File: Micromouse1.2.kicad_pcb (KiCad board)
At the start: 2 copper layers, 42 x 17 mm, 113 parts, among them J1 USB_B, P1 CONN_01X4, U1 BAT54C, U10 2X3Header, U11 ULN2003APWR, U12 SMT_0540-S-R, U13 splitter, U14 ferrite, U15 LMZ21701, U16 JST_Connector, U17 Switch_micromouse, U18 LMZ21701, U19 splitter, U2 TC4427, U20 TPD3S014, U21 MKL02Z32VFG4, U22 LP38691, U23 MK66FX1M0, U24 Test_Point, U25 Test_Point, U26 Test_Point, U27 Test_Point, U28 Test_Point, U29 Test_Point, U3 ferrite, U30 Test_Point, U4 TC4427, U5 ferrite, U6 BAT54C, U7 ZXMHC3F381N8, U8 ZXMHC3F381N8, U9 2X3Header, Y1 Crystal_16MHz, Y2 32.768MHz

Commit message: finished floor planning
-replaced the TC4427 and H brige by a single DRV8833 chip
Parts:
- removed C3: 0.1uF, Capacitors_SMD:C_0603
- removed D7: D, Diodes_SMD:D_0603
- removed U12: SMT_0540-S-R, micromouse:Buzzer_SMT-0540-S-R
- removed U4: TC4427, micromouse:TC4427_MSOP8
- removed U7, U8: ZXMHC3F381N8, micromouse:ZXMHC3F381N8
- added C32: 10nF, Capacitors_SMD:C_0603, F.Cu at (122.6, 71.3)
- added C33: 0.1uF, Capacitors_SMD:C_0603, F.Cu at (122.6, 69.8)
- added C34: C, Capacitors_SMD:C_0603, F.Cu at (118.6, 67.7)
- added C35: C, Capacitors_SMD:C_0402, F.Cu at (118.8, 124.5)
- added U31: MPU-6500, micromouse:MPU-6500, F.Cu at (118.7, 70.7)
- added U32: Motor_mount, micromouse:Motor_mount, F.Cu at (140.3, 87.3)
- C1: value 0.1uF -> 100uF
- C10, C12: footprint Resistors_SMD:R_0805 -> micromouse:R_0805
- C11, C14, C17, C21, C22, C23, C25, C26, C28: footprint Capacitors_SMD:C_0402 -> micromouse:C_0402
- C13, C15: footprint Capacitors_SMD:C_0805 -> micromouse:C_0805
- C16, C18, C19, C24, C27, C29, U3: footprint Capacitors_SMD:C_0402 -> micromouse:C_0603
- C2: value 100uF -> 10uF; footprint Capacitors_SMD:C_0603 -> Capacitors_SMD:C_0805
- C20: footprint Capacitors_SMD:C_1206 -> micromouse:C_1206
- C4: value 100uF -> 0.1uF
- D1, D2, D3, D4, D5, D6: footprint micromouse:IR-Reciver -> micromouse:IR_Reciver
- D10, D11, D12, D13, D8, D9: footprint micromouse:IR-Emitter -> micromouse:IR_Emitter
- J1: footprint micromouse:USB_B -> micromouse:USB_Micro-B
- R1, R2, R3, R4, R5, R6, R7, R8: footprint Resistors_SMD:R_0603 -> Capacitors_SMD:C_0402
- R15, R16, R17, R18, R19, R20: footprint Resistors_SMD:R_0603 -> micromouse:C_0402
- R21, R22, R23, R25, R26, R27, R39, R40: footprint Resistors_SMD:R_0402 -> micromouse:R_0402
- R24, R28, R29: footprint Resistors_SMD:R_0603 -> micromouse:R_0603
- U11: footprint micromouse:ULN2003APWR -> micromouse:ULN2003V12
- U13: value splitter -> Motor_mount; footprint micromouse:spliter -> micromouse:Motor_mount
- U14, U5: footprint Capacitors_SMD:C_0402 -> micromouse:R_0402
- U15: footprint MicromouseFootprint:LMZ21701 -> micromouse:LMZ21701
- U16: footprint Capacitors_SMD:C_0402 -> micromouse:JST_Connector
- U2: value TC4427 -> DRV8833; footprint micromouse:TC4427_MSOP8 -> micromouse:DRV8833
- moved R28 152.6 mm to (101.4, 76.7)
- moved R29 152.4 mm to (101.5, 71.8), turned to 180 degrees
- moved U13 146.4 mm to (97.3, 87.3), turned to 270 degrees
- moved R24 118.9 mm to (135.0, 76.2), turned to 90 degrees
- moved U19 77.9 mm to (134.1, 103.8), turned to 90 degrees
- moved C6 63.7 mm to (110.3, 45.3)
- moved P1 63.5 mm to (25.5, 58.6), turned to 270 degrees
- moved J1 52.4 mm to (133.0, 110.1), turned to 0 degrees
- moved C9 51.9 mm to (118.1, 38.0)
- moved D6 51.4 mm to (151.8, 59.9), turned to 174.7 degrees
- moved C8 51.1 mm to (119.5, 38.0), turned to 270 degrees
- moved D1 49.5 mm to (88.1, 59.2), turned to 184.3 degrees
- moved D8 46.9 mm to (93.5, 56.0), turned to 184.3 degrees
- moved C12 46.8 mm to (131.4, 71.4), turned to 180 degrees
- moved U24 46.3 mm to (134.2, 71.6), turned to 180 degrees
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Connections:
- C1 pad 1: V_BAT -> VBAT
- C1 pad 2: GNDM -> GNDD
- C2 pad 1: V_BAT -> VBAT
- C2 pad 2: GNDM -> GNDD
- C21 pad 2: GND -> GNDD
- C22 pad 2: GND -> GNDD
- C23 pad 2: GND -> GNDD
- C25 pad 2: GND -> GNDD
- C27 pad 2: GND -> GNDD
- C29 pad 2: GND -> GNDD
- C30 pad 1: V3.3 -> V1.8
- C31 pad 1: V3.3 -> V1.8
- C4 pad 1: V_BAT -> VBAT
- C4 pad 2: GNDM -> GNDD
- C6 pad 1: V3.3 -> V1.8
- C7 pad 1: V3.3 -> V1.8
- C8 pad 1: V3.3 -> V1.8
- C9 pad 1: V3.3 -> V1.8
- D10 pad 2: V3.3 -> V1.8
- D11 pad 2: V3.3 -> V1.8
- D12 pad 2: V3.3 -> V1.8
- D13 pad 2: V3.3 -> V1.8
- D8 pad 2: V3.3 -> V1.8
- D9 pad 2: V3.3 -> V1.8
- J1 pad 1: Net-(C16-Pad1) -> Net-(J1-Pad1)
- J1 pad 4: GND -> Net-(J1-Pad4)
- J1 pad 5: GND -> Net-(J1-Pad5)
- L1 pad 1: Net-(C15-Pad1) -> Net-(L1-Pad1)
- P1 pad 3: GND -> Net-(P1-Pad3)
- R29 pad 1: Net-(L1-Pad2) -> Net-(R29-Pad1)
- R37 pad 2: Net-(J1-Pad3) -> Net-(R37-Pad2)
- R38 pad 2: Net-(J1-Pad2) -> Net-(R38-Pad2)
- R5 pad 1: Net-(R1-Pad1) -> Net-(R3-Pad1)
- R6 pad 1: Net-(R3-Pad1) -> GNDD
- R6 pad 2: GNDD -> Net-(R2-Pad1)
- R7 pad 1: Net-(R2-Pad1) -> Net-(R4-Pad1)
- R8 pad 1: Net-(R4-Pad1) -> GNDD
- R8 pad 2: GNDD -> Net-(R1-Pad1)
- U1 pad 1: Net-(C17-Pad1) -> Net-(C22-Pad1)
- U1 pad 2: Net-(C22-Pad1) -> Net-(U1-Pad2)
- U1 pad 3: Net-(U1-Pad3) -> Net-(C17-Pad1)
- U19 pad 2: Net-(U19-Pad2) -> GNDA
- U2 pad 1: Net-(U2-Pad1) -> Net-(R30-Pad1)
- U2 pad 2: Net-(R1-Pad1) -> Net-(U2-Pad2)
- U2 pad 3: GNDM -> Net-(U10-Pad4)
- U2 pad 4: Net-(R2-Pad1) -> Net-(R30-Pad1)
- U2 pad 5: Net-(U2-Pad5) -> Net-(U10-Pad3)
- U2 pad 6: V_BAT -> Net-(U2-Pad6)
- U2 pad 7: Net-(U2-Pad7) -> Net-(R3-Pad1)
- U2 pad 8: Net-(U2-Pad8) -> Net-(R4-Pad1)
- U20 pad 1: Net-(C21-Pad1) -> Net-(R40-Pad1)
- U20 pad 3: Net-(R40-Pad1) -> Net-(C21-Pad1)
- U22 pad 2: GND -> GNDD
- U26 pad 1: Net-(L1-Pad2) -> Net-(R29-Pad1)
- U27 pad 1: Net-(R1-Pad1) -> Net-(R2-Pad1)
- U28 pad 1: Net-(R3-Pad1) -> Net-(R4-Pad1)
- U29 pad 1: Net-(R2-Pad1) -> Net-(R1-Pad1)
- U30 pad 1: Net-(R4-Pad1) -> Net-(R3-Pad1)
- U6 pad 1: Net-(C21-Pad1) -> Net-(U3-Pad2)
- U6 pad 3: Net-(U3-Pad2) -> Net-(C21-Pad1)
- U9 pad 3: Net-(U7-Pad2) -> Net-(U2-Pad16)
- U9 pad 4: Net-(U7-Pad6) -> Net-(U2-Pad2)
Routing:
- net Net-(C22-Pad1): track 0.00 -> 34.6 mm, vias 0 -> 1
- net GNDD: track 1.20 -> 35.2 mm, vias 4 -> 5
- net Net-(R37-Pad1): track 0.00 -> 16.0 mm
- net Net-(U20-Pad6): track 0.00 -> 15.8 mm, vias 0 -> 2
- net Net-(C28-Pad1): track 0.00 -> 13.8 mm, vias 0 -> 1
- net Net-(U23-PadM7): track 0.00 -> 11.5 mm
- net GNDM: track 10.9 -> 0.00 mm
- net Net-(U7-Pad6): track 10.8 -> 0.00 mm
- net Net-(C21-Pad1): track 0.00 -> 10.3 mm
- net Net-(U10-Pad4): track 10.2 -> 0.00 mm
- net Net-(C18-Pad1): track 0.00 -> 9.29 mm, vias 0 -> 2
- net V_BAT: track 14.2 -> 23.0 mm
- net Net-(C19-Pad1): track 0.00 -> 7.91 mm
- net Net-(U2-Pad7): track 7.05 -> 0.00 mm
- net Net-(U2-Pad5): track 6.78 -> 0.00 mm
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- added copper zone on F.Cu, net Net-(C22-Pad1)
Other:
- board size 42 x 17 mm -> 70.4 x 87.9 mm
- rule trace_min: 0.2 -> 0.1
- rule via_min_size: 0.4 -> 0.3

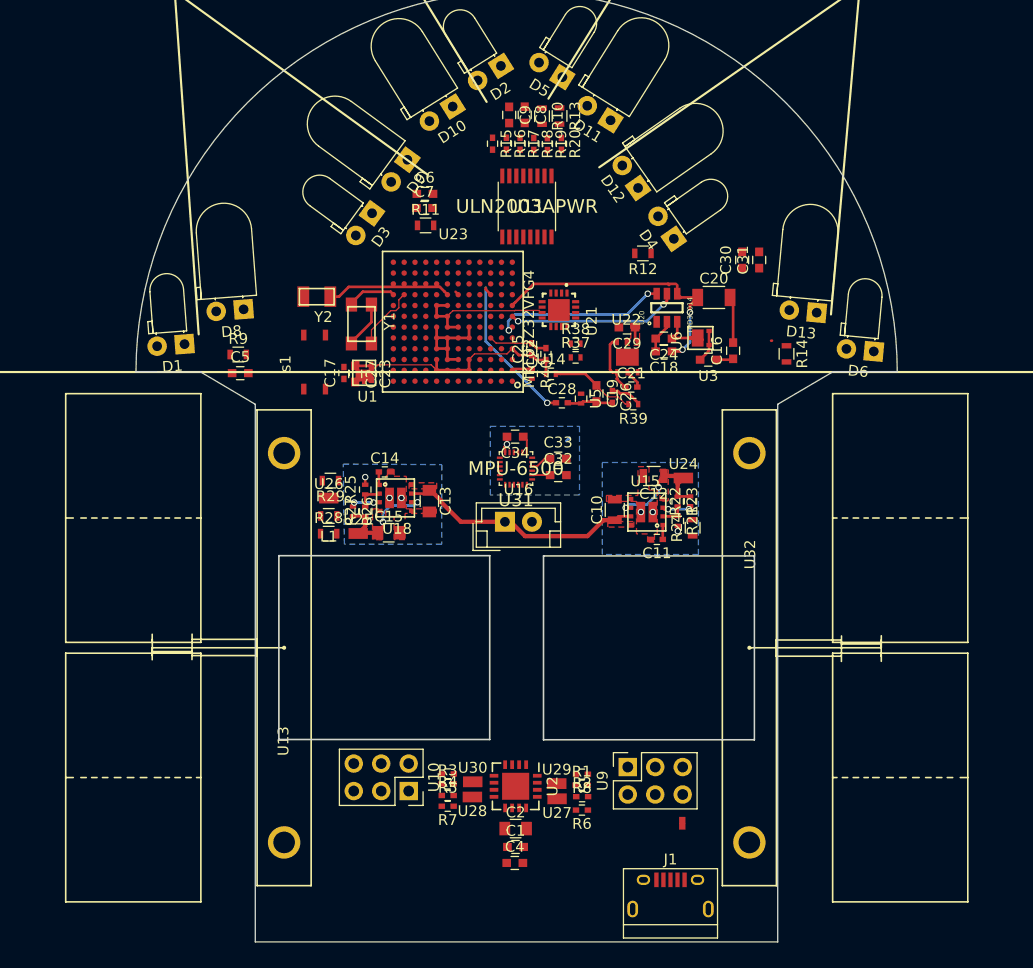
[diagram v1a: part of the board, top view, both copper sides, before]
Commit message: made 3D wheel and Tire setup
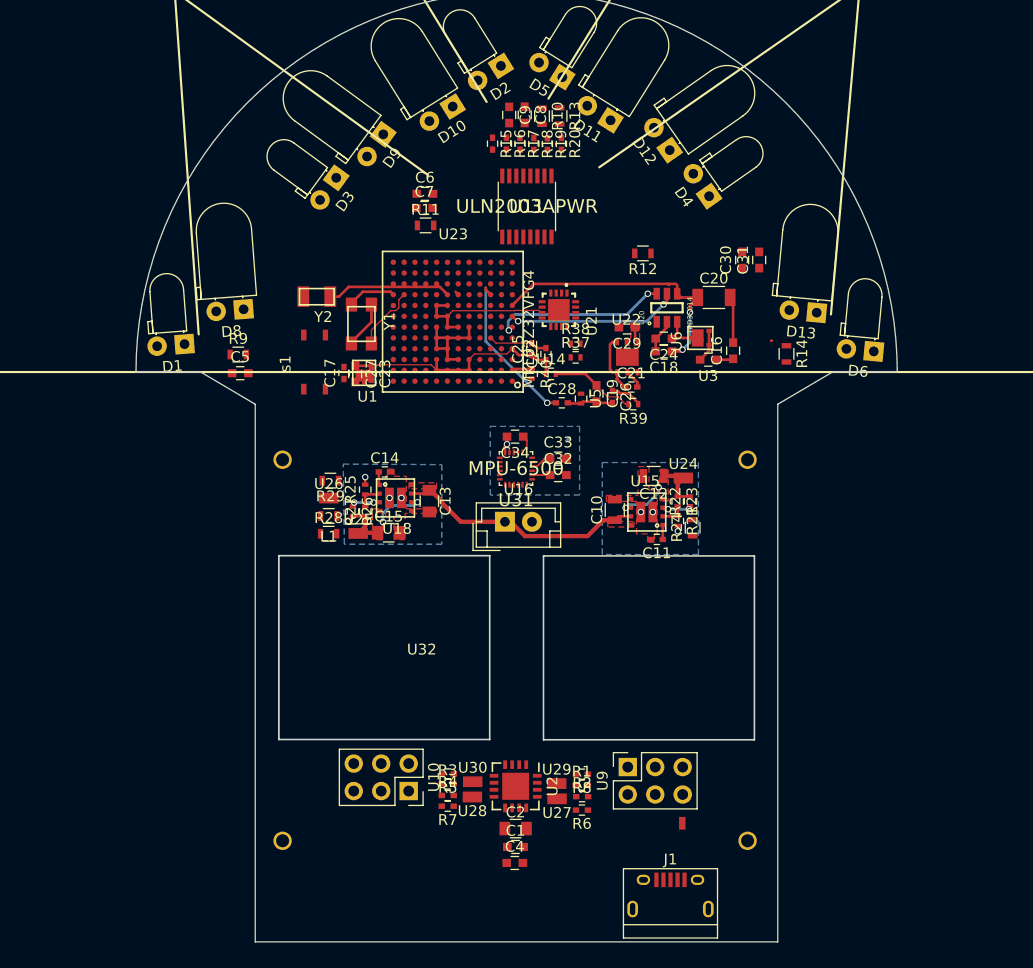
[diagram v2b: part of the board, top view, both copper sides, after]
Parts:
- removed U13: Motor_mount, micromouse:Motor_mount
- R21: value 44.2k -> 150K
- R23: value 232k -> 226K
- U10, U9: value 2X3Header -> CONN_02X03
- moved U32 21.7 mm to (118.6, 87.5), turned to 180 degrees
- moved D4 5.12 mm to (136.6, 45.5)
- moved D3 4.66 mm to (102.1, 43.8)
- moved D12 4.56 mm to (132.9, 41.2)
- moved D9 3.24 mm to (106.4, 39.8)
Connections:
- L1 pad 1: Net-(L1-Pad1) -> Net-(C15-Pad1)
- R24 pad 1: +5V -> 2V
- R29 pad 1: Net-(R29-Pad1) -> Net-(L1-Pad2)
- U10 pad 2: +5V -> L_CH_B
- U10 pad 3: Net-(U10-Pad3) -> +5V
- U10 pad 4: Net-(U10-Pad4) -> GNDD
- U10 pad 5: GNDD -> Net-(U10-Pad5)
- U10 pad 6: L_CH_B -> Net-(U10-Pad6)
- U2 pad 3: Net-(U10-Pad4) -> Net-(U10-Pad6)
- U2 pad 5: Net-(U10-Pad3) -> Net-(U10-Pad5)
- U26 pad 1: Net-(R29-Pad1) -> Net-(L1-Pad2)
- U9 pad 2: +5V -> R_CH_B
- U9 pad 3: Net-(U2-Pad16) -> +5V
- U9 pad 4: Net-(U2-Pad2) -> GNDD
- U9 pad 5: GNDD -> Net-(U2-Pad16)
- U9 pad 6: R_CH_B -> Net-(U2-Pad2)

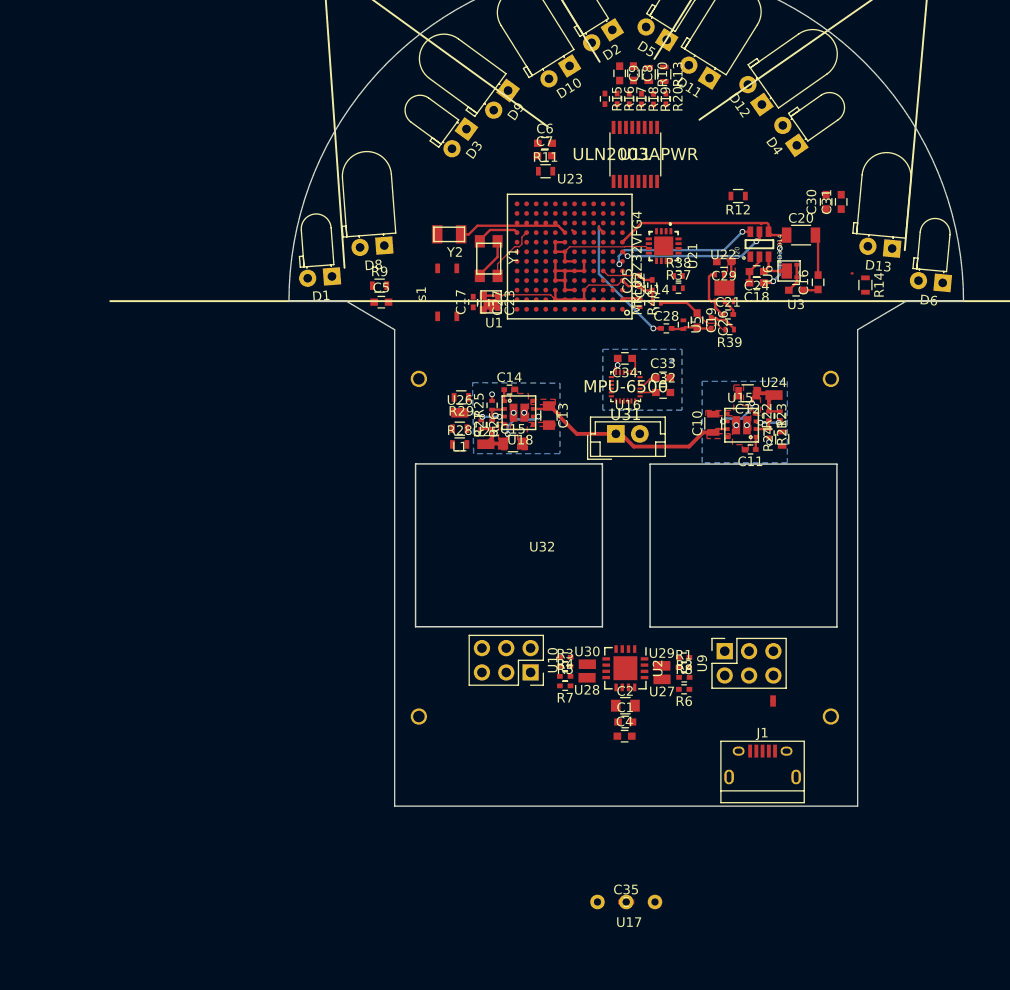
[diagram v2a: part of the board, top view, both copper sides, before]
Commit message: Change of direction
- I am changing my MCU from mk66fx1m0vmd18 to mk20dx256vlh7 as the QFN  package pcb layout is too expensive to manufacture and the  144 LQFP is takes too much real estate
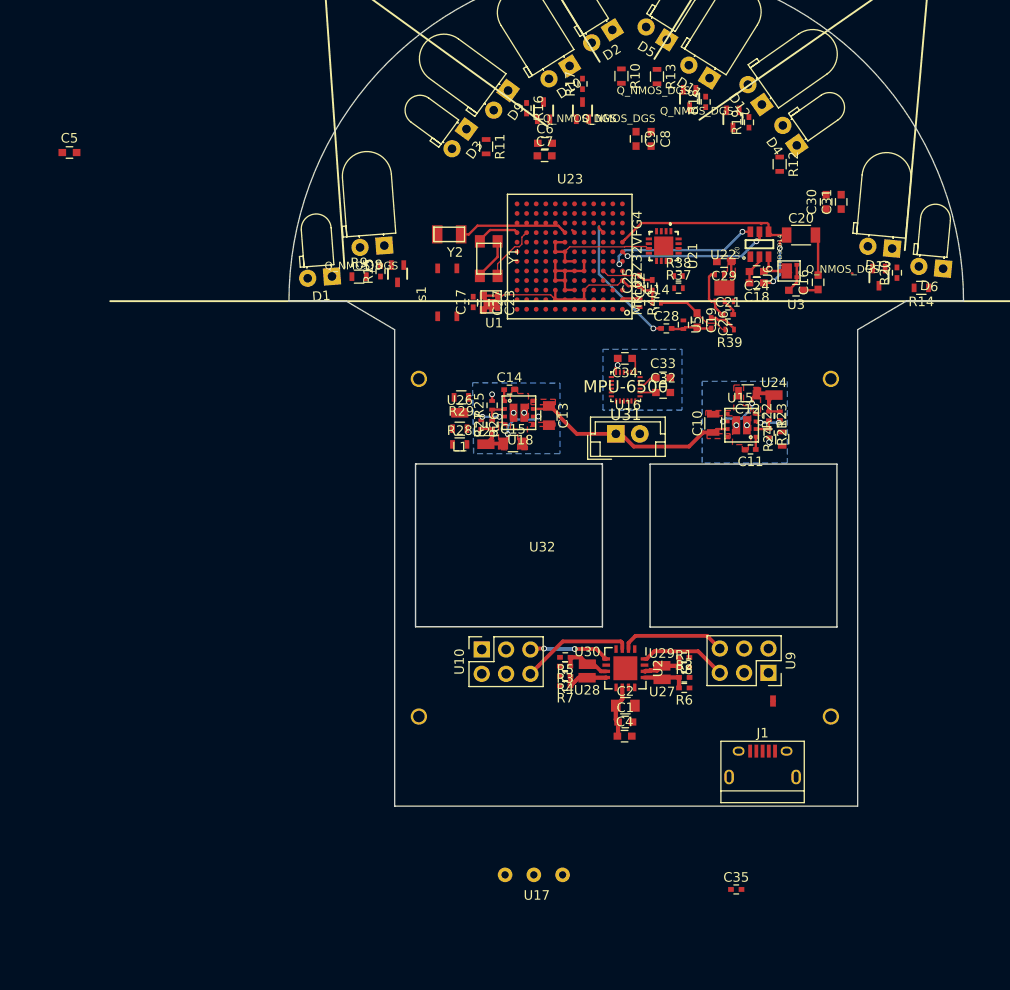
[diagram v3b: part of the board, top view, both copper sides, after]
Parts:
- removed U11: ULN2003APWR, micromouse:ULN2003V12
- added Q1: Q_NMOS_DGS, micromouse:DMG1012UW, F.Cu at (94.9, 58.9)
- added Q2: Q_NMOS_DGS, micromouse:DMG1012UW, F.Cu at (110.1, 41.9)
- added Q3: Q_NMOS_DGS, micromouse:DMG1012UW, F.Cu at (114.2, 41.9)
- added Q4: Q_NMOS_DGS, micromouse:DMG1012UW, F.Cu at (125.4, 40.6)
- added Q5: Q_NMOS_DGS, micromouse:DMG1012UW, F.Cu at (129.9, 42.7)
- added Q6: Q_NMOS_DGS, micromouse:DMG1012UW, F.Cu at (145.1, 59.3)
- moved C5 36.1 mm to (60.7, 46.3)
- moved R20 30.2 mm to (147.0, 58.8), turned to 90 degrees
- moved R15 29.5 mm to (93.1, 58.6), turned to 90 degrees
- moved C35 11.6 mm to (130.2, 123.2)
- moved R19 10.3 mm to (131.6, 43.1), turned to 90 degrees
- moved U17 10.1 mm to (109.1, 121.6)
- moved R16 9.51 mm to (108.4, 41.6)
- moved C8 7.09 mm to (121.4, 44.8)
- moved C9 7.05 mm to (119.8, 44.8)
- moved R11 6.71 mm to (104.1, 45.6), turned to 270 degrees
- moved R18 6.70 mm to (127.1, 41.0), turned to 90 degrees
- moved R14 5.84 mm to (149.6, 60.4), turned to 180 degrees
- moved U10 5.63 mm to (103.7, 98.1), turned to 90 degrees
- moved R12 5.46 mm to (134.8, 47.5), turned to 270 degrees
- moved R17 5.12 mm to (114.2, 39.1), turned to 90 degrees
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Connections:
- C30 pad 2: Net-(C30-Pad2) -> GNDD
- C31 pad 2: Net-(C30-Pad2) -> GNDD
- R15 pad 1: Net-(D8-Pad1) -> Net-(Q1-Pad1)
- R15 pad 2: Net-(R15-Pad2) -> Net-(D8-Pad1)
- R16 pad 1: Net-(D9-Pad1) -> Net-(Q2-Pad1)
- R16 pad 2: Net-(R16-Pad2) -> Net-(D9-Pad1)
- R17 pad 1: Net-(D10-Pad1) -> Net-(Q3-Pad1)
- R17 pad 2: Net-(R17-Pad2) -> Net-(D10-Pad1)
- R18 pad 1: Net-(D11-Pad1) -> Net-(Q4-Pad1)
- R18 pad 2: Net-(R18-Pad2) -> Net-(D11-Pad1)
- R19 pad 1: Net-(D12-Pad1) -> Net-(Q5-Pad1)
- R19 pad 2: Net-(R19-Pad2) -> Net-(D12-Pad1)
- R20 pad 1: Net-(D13-Pad1) -> Net-(Q6-Pad1)
- R20 pad 2: Net-(R20-Pad2) -> Net-(D13-Pad1)
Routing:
- net Net-(U10-Pad6): track 0.00 -> 11.7 mm
- net Net-(U2-Pad2): track 0.00 -> 11.0 mm
- net Net-(U2-Pad16): track 0.00 -> 9.11 mm
- net Net-(U10-Pad5): track 0.00 -> 8.63 mm, vias 0 -> 2
- net VBAT: track 0.00 -> 5.50 mm
- net Net-(R3-Pad1): track 0.00 -> 5.26 mm
- net Net-(R4-Pad1): track 0.00 -> 5.08 mm
- net Net-(R1-Pad1): track 0.00 -> 4.88 mm
- net Net-(R2-Pad1): track 0.00 -> 4.86 mm
